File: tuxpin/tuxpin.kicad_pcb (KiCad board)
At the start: 2 copper layers, 35.1 x 46.9 mm, 23 parts, among them Q1 BC817, Q2 BC817, Q3 BC817, Q4 BC817, Q5 BC817, Q6 BC817, U1 PST-540, U2 MAX16054AZT

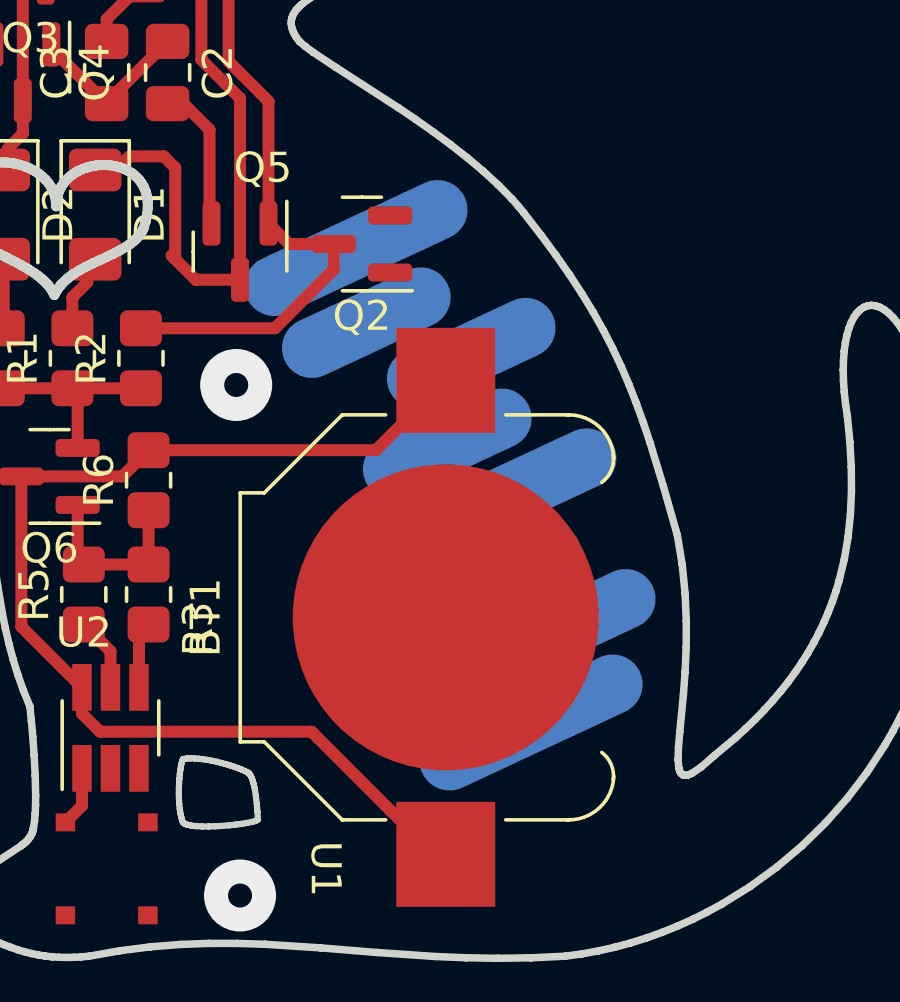
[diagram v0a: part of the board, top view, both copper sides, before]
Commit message: added conductive button
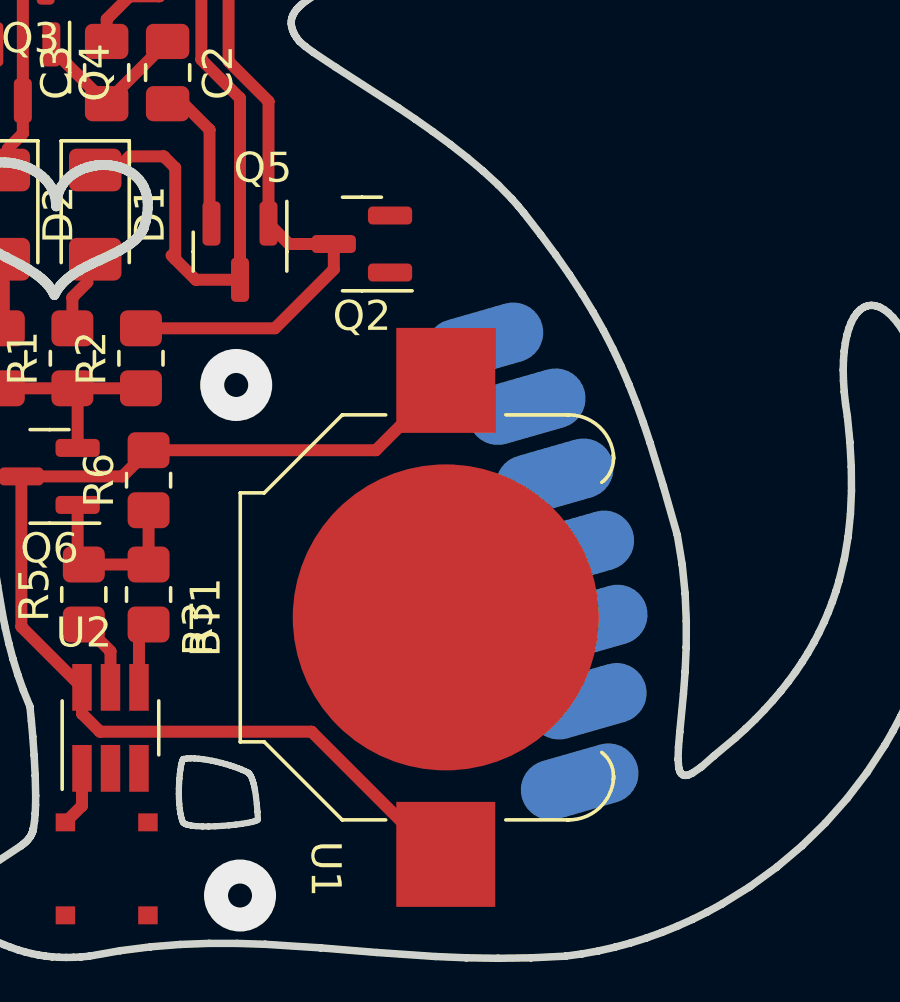
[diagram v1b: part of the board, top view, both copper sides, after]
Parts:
- moved CB1 5.16 mm to (175.4, 108.0), turned to 16 degrees
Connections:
- U1 pad 4: (no net) -> unconnected-(U1-Pad4)

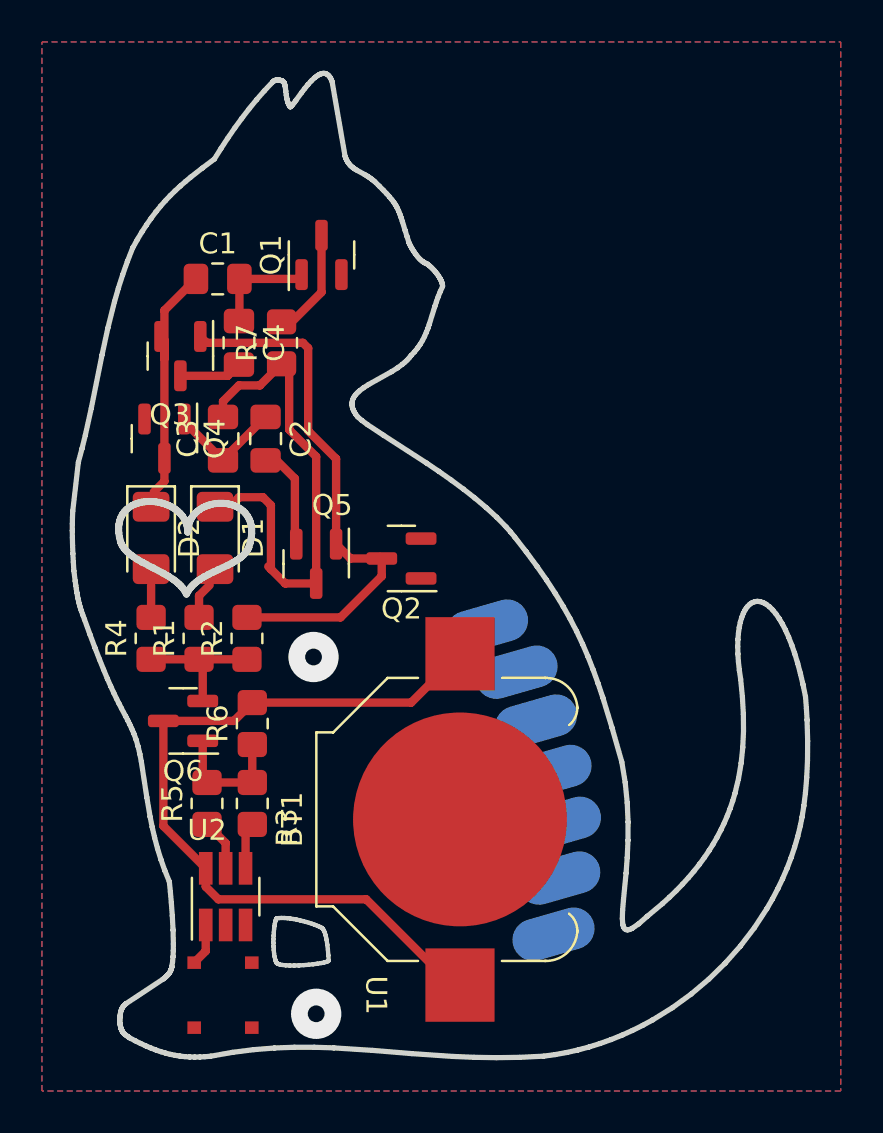
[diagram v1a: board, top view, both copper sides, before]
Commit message: first version of pcb -> ERC doesn't pass
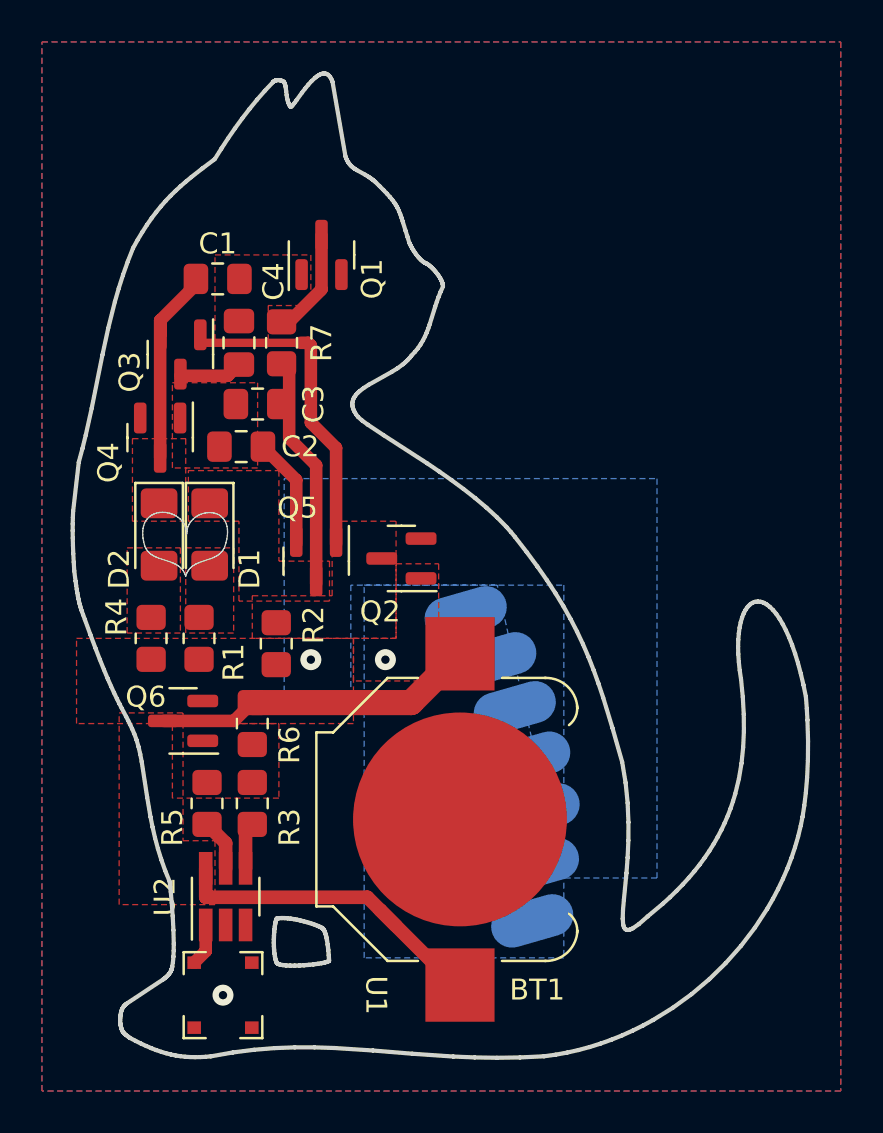
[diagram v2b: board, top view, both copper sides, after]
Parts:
- moved C3 2.33 mm to (157.5, 93.0), turned to 0 degrees
- moved R2 1.42 mm to (158.4, 104.4)
- moved C2 1.23 mm to (156.7, 95.0), turned to 0 degrees
- moved CB1 1.20 mm to (174.4, 107.4)
- moved D2 0.41 mm to (152.8, 99.2)
- moved D1 0.30 mm to (155.2, 99.2)
- moved Q4 0.21 mm to (152.8, 94.6)
- moved Q5 0.13 mm to (160.3, 100.5)
- moved Q3 0.08 mm to (153.8, 90.6)
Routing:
- net Net-(D1-K): track 23.0 -> 11.2 mm
- net Net-(Q2-C): track 25.9 -> 15.0 mm
- net VCC: track 6.74 -> 0.00 mm, vias 0 -> 1
- net Net-(Q6-B): track 6.04 -> 0.00 mm
- net Net-(Q4-B): track 5.66 -> 0.00 mm
- net Net-(Q1-C): track 5.21 -> 10.3 mm
- net Net-(Q1-B): track 5.07 -> 0.03 mm
- net Net-(D2-K): track 12.0 -> 9.92 mm
- net Net-(D1-A): track 1.75 -> 0.00 mm
- net Net-(D2-A): track 1.54 -> 0.00 mm
- net +3V0: track 36.6 -> 35.8 mm
- added copper zone on F.Cu, net +3V0
- added copper zone on F.Cu, net Net-(D1-A)
- added copper zone on F.Cu, net Net-(D1-K)
- added copper zone on F.Cu, net Net-(D2-A)
- added copper zone on F.Cu, net Net-(D2-K)
- added copper zone on F.Cu, net Net-(Q1-B)
- added copper zone on B.Cu, net Net-(Q2-B)
- added copper zone on F.Cu, net Net-(Q2-B)
- added copper zone on F.Cu, net Net-(Q2-C)
- added copper zone on F.Cu, net Net-(Q4-B)
- added copper zone on F.Cu, net Net-(Q6-B)
- added copper zone on B.Cu, net VCC
- added copper zone on F.Cu, net VCC
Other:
- outline, holes or cut-outs redrawn

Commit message: drc almost without errors - library error battery holder
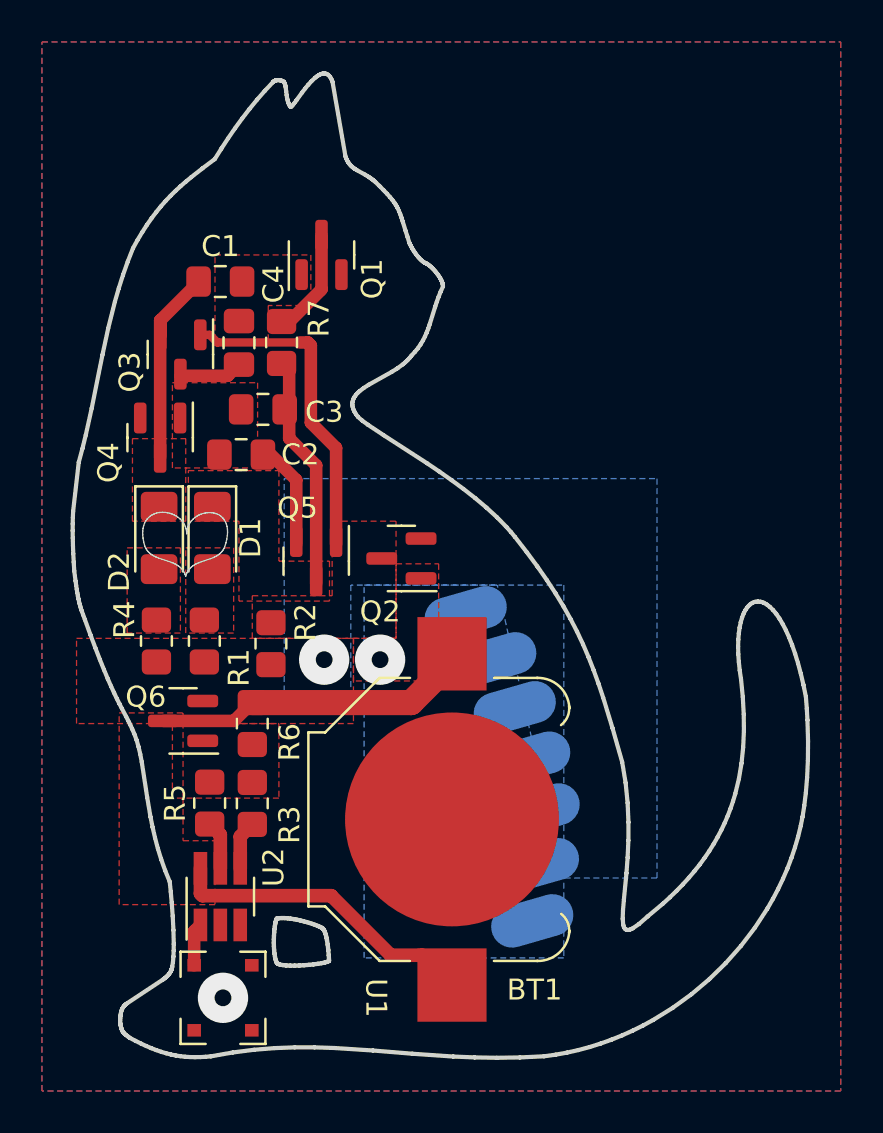
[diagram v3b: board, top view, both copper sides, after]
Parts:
- moved BT1 0.38 mm to (166.8, 112.8)
- moved C2 0.38 mm to (156.7, 95.4)
- moved C3 0.36 mm to (157.7, 93.2)
- moved R1 0.28 mm to (154.9, 104.3)
- moved R4 0.28 mm to (152.7, 104.3)
- moved R2 0.25 mm to (158.1, 104.4)
- moved U2 0.25 mm to (155.7, 116.5)
- moved D1 0.21 mm to (155.3, 99.4)
- moved C1 0.18 mm to (155.7, 87.1)
- moved D2 0.16 mm to (152.8, 99.4)
- moved R5 0.13 mm to (155.2, 112.0)
- moved U1 0.13 mm to (155.8, 121.3)
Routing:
- net +3V0: track 35.8 -> 30.5 mm
